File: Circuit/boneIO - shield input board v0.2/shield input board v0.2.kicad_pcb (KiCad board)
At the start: 2 copper layers, 38.1 x 17.5 mm, 22 parts, among them J12 ZW_VCC, J13 ZW_GND, Q1 BC817, Q2 BC807, Q3 BC817, Q4 BC807, U1 PC817, U2 PC817, U3 PC817, U4 PC817, U5 PC817, U6 PC817

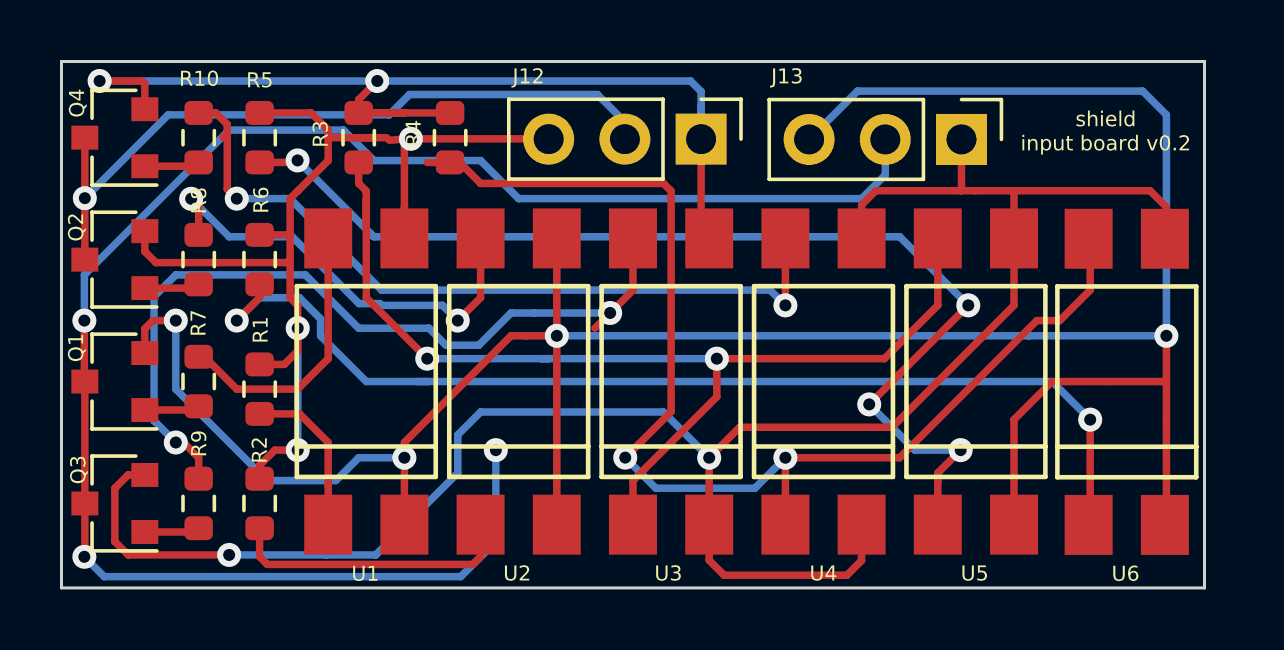
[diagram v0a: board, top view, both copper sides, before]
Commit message: reduced PCB
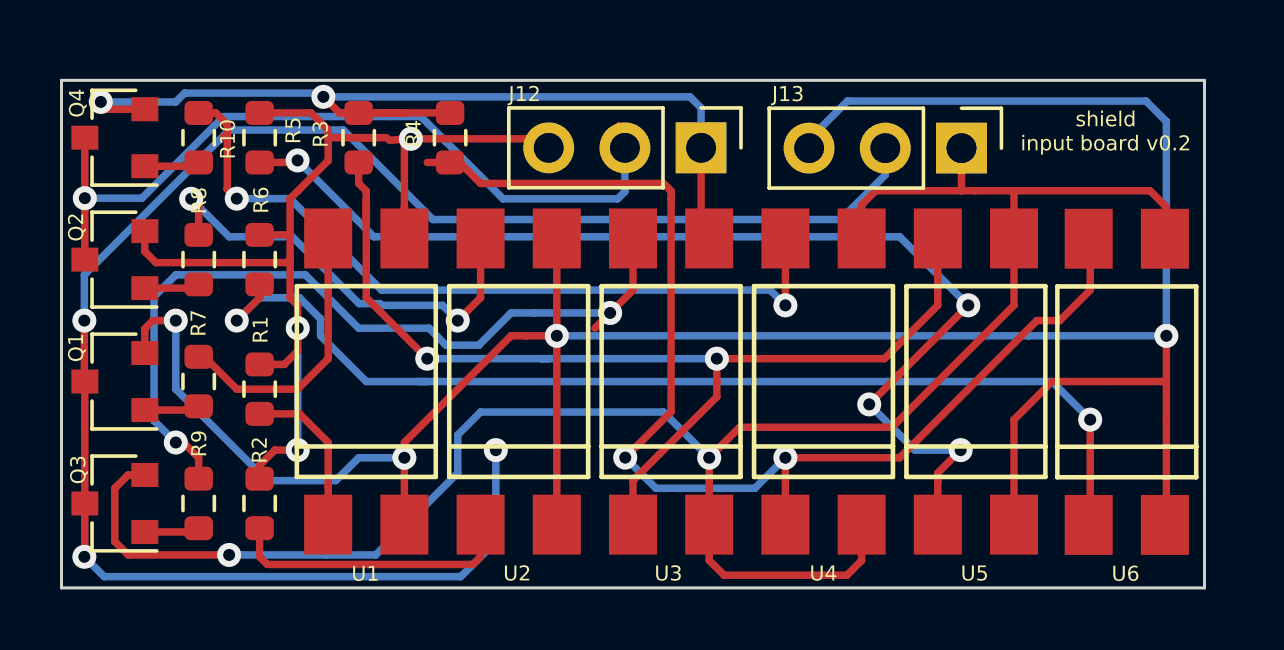
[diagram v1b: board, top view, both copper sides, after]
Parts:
- moved J13 0.29 mm to (210.3, 63.3)
- moved J12 0.29 mm to (201.7, 63.3)
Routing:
- net +24V: track 34.6 -> 32.8 mm
- net VDD: track 25.0 -> 26.4 mm
- net GNDA: track 58.1 -> 58.7 mm
- added copper zone on B.Cu, net GND
- added copper zone on F.Cu, net GND
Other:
- board size 38.1 x 17.5 mm -> 38.1 x 16.9 mm
